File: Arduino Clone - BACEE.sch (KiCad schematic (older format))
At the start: 13 parts, among them U1 24LC1025, U2 24LC1025, U3 DS1337_AF, U4 ATMEGA328P-AU, Y1 Crystal, Y2 Crystal

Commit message: associations
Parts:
- BT1: value Battery -> Battery 3V; footprint (none) -> Connector_PinHeader_2.54mm:PinHeader_1x02_P2.54mm_Vertical
- C1, C2: value C -> 22pF; footprint (none) -> Capacitor_SMD:C_0805_2012Metric_Pad1.15x1.40mm_HandSolder
- C3: value CP -> 10uF; footprint (none) -> Capacitor_SMD:C_0805_2012Metric_Pad1.15x1.40mm_HandSolder
- D1: footprint (none) -> LED_SMD:LED_0805_2012Metric_Pad1.15x1.40mm_HandSolder
- R1: value R -> 330Ohms; footprint (none) -> Resistor_SMD:R_0805_2012Metric_Pad1.15x1.40mm_HandSolder
- R2: value R -> 10kOhms; footprint (none) -> Resistor_SMD:R_0805_2012Metric_Pad1.15x1.40mm_HandSolder
- U1, U2: footprint (none) -> Package_SO:SOIJ-8_5.3x5.3mm_P1.27mm
- U3: value DS1337_AF -> DS13375+; footprint (none) -> Package_SO:SO-8_5.3x6.2mm_P1.27mm
- Y1: value Crystal -> Crystal 32Mhz; footprint (none) -> Crystal:Crystal_SMD_MicroCrystal_CC7V-T1A-2Pin_3.2x1.5mm
- Y2: value Crystal -> Crystal 16Mhz; footprint (none) -> Crystal:Crystal_SMD_5032-2Pin_5.0x3.2mm_HandSoldering
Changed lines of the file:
@@
 P 9100 2250
 F 0 "BT1" H 9208 2296 50  0000 L CNN
-F 1 "Battery" H 9208 2205 50  0000 L CNN
-F 2 "" V 9100 2310 50  0001 C CNN
+F 1 "Battery 3V" H 9208 2205 50  0000 L CNN
+F 2 "Connector_PinHeader_2.54mm:PinHeader_1x02_P2.54mm_Vertical" V 9100 2310 50  0001 C CNN
 F 3 "~" V 9100 2310 50  0001 C CNN
 	1    9100 2250
@@
 P 5300 1850
 F 0 "C1" H 5415 1896 50  0000 L CNN
-F 1 "C" H 5415 1805 50  0000 L CNN
-F 2 "" H 5338 1700 50  0001 C CNN
+F 1 "22pF" H 5415 1805 50  0000 L CNN
+F 2 "Capacitor_SMD:C_0805_2012Metric_Pad1.15x1.40mm_HandSolder" H 5338 1700 50  0001 C CNN
 F 3 "~" H 5300 1850 50  0001 C CNN
 	1    5300 1850
@@
 P 5300 2250
 F 0 "C2" H 5415 2296 50  0000 L CNN
-F 1 "C" H 5415 2205 50  0000 L CNN
-F 2 "" H 5338 2100 50  0001 C CNN
+F 1 "22pF" H 5415 2205 50  0000 L CNN
+F 2 "Capacitor_SMD:C_0805_2012Metric_Pad1.15x1.40mm_HandSolder" H 5338 2100 50  0001 C CNN
 F 3 "~" H 5300 2250 50  0001 C CNN
 	1    5300 2250
@@
 P 9600 3100
 F 0 "C3" H 9718 3146 50  0000 L CNN
-F 1 "CP" H 9718 3055 50  0000 L CNN
-F 2 "" H 9638 2950 50  0001 C CNN
+F 1 "10uF" H 9718 3055 50  0000 L CNN
+F 2 "Capacitor_SMD:C_0805_2012Metric_Pad1.15x1.40mm_HandSolder" H 9638 2950 50  0001 C CNN
 F 3 "~" H 9600 3100 50  0001 C CNN
 	1    9600 3100
@@
 F 0 "D1" H 5843 2866 50  0000 C CNN
 F 1 "LED" H 5843 2775 50  0000 C CNN
-F 2 "" H 5850 2650 50  0001 C CNN
+F 2 "LED_SMD:LED_0805_2012Metric_Pad1.15x1.40mm_HandSolder" H 5850 2650 50  0001 C CNN
 F 3 "~" H 5850 2650 50  0001 C CNN
 	1    5850 2650
@@
 P 5400 2950
 F 0 "R1" H 5470 2996 50  0000 L CNN
-F 1 "R" H 5470 2905 50  0000 L CNN
-F 2 "" V 5330 2950 50  0001 C CNN
+F 1 "330Ohms" H 5470 2905 50  0000 L CNN
+F 2 "Resistor_SMD:R_0805_2012Metric_Pad1.15x1.40mm_HandSolder" V 5330 2950 50  0001 C CNN
 F 3 "~" H 5400 2950 50  0001 C CNN
 	1    5400 2950
@@
 P 5400 3350
 F 0 "R2" H 5470 3396 50  0000 L CNN
-F 1 "R" H 5470 3305 50  0000 L CNN
-F 2 "" V 5330 3350 50  0001 C CNN
+F 1 "10kOhms" H 5470 3305 50  0000 L CNN
+F 2 "Resistor_SMD:R_0805_2012Metric_Pad1.15x1.40mm_HandSolder" V 5330 3350 50  0001 C CNN
 F 3 "~" H 5400 3350 50  0001 C CNN
 	1    5400 3350
@@
 F 0 "U1" H 2100 5831 50  0000 C CNN
 F 1 "24LC1025" H 2100 5740 50  0000 C CNN
-F 2 "" H 2100 5350 50  0001 C CNN
+F 2 "Package_SO:SOIJ-8_5.3x5.3mm_P1.27mm" H 2100 5350 50  0001 C CNN
 F 3 "http://ww1.microchip.com/downloads/en/DeviceDoc/21941B.pdf" H 2100 5350 50  0001 C CNN
 	1    2100 5350
@@
 P 2550 2250
 F 0 "U3" H 2525 2881 50  0000 C CNN
-F 1 "DS1337_AF" H 2525 2790 50  0000 C CNN
-F 2 "" H 2550 2250 50  0001 C CNN
+F 1 "DS13375+" H 2525 2790 50  0000 C CNN
+F 2 "Package_SO:SO-8_5.3x6.2mm_P1.27mm" H 2550 2250 50  0001 C CNN
 F 3 "https://datasheets.maximintegrated.com/en/ds/DS1337-DS1337C.pdf" H 2550 2250 50  0001 C CNN
 	1    2550 2250
@@
 P 1600 2000
 F 0 "Y1" H 1600 2268 50  0000 C CNN
-F 1 "Crystal" H 1600 2177 50  0000 C CNN
-F 2 "" H 1600 2000 50  0001 C CNN
+F 1 "Crystal 32Mhz" H 1600 2177 50  0000 C CNN
+F 2 "Crystal:Crystal_SMD_MicroCrystal_CC7V-T1A-2Pin_3.2x1.5mm" H 1600 2000 50  0001 C CNN
 F 3 "~" H 1600 2000 50  0001 C CNN
 	1    1600 2000
@@
 P 5750 2100
 F 0 "Y2" V 5704 2231 50  0000 L CNN
-F 1 "Crystal" V 5795 2231 50  0000 L CNN
-F 2 "" H 5750 2100 50  0001 C CNN
+F 1 "Crystal 16Mhz" V 5795 2231 50  0000 L CNN
+F 2 "Crystal:Crystal_SMD_5032-2Pin_5.0x3.2mm_HandSoldering" H 5750 2100 50  0001 C CNN
 F 3 "~" H 5750 2100 50  0001 C CNN
 	1    5750 2100
@@
 F 0 "U2" H 2100 6981 50  0000 C CNN
 F 1 "24LC1025" H 2100 6890 50  0000 C CNN
-F 2 "" H 2100 6500 50  0001 C CNN
+F 2 "Package_SO:SOIJ-8_5.3x5.3mm_P1.27mm" H 2100 6500 50  0001 C CNN
 F 3 "http://ww1.microchip.com/downloads/en/DeviceDoc/21941B.pdf" H 2100 6500 50  0001 C CNN
 	1    2100 6500

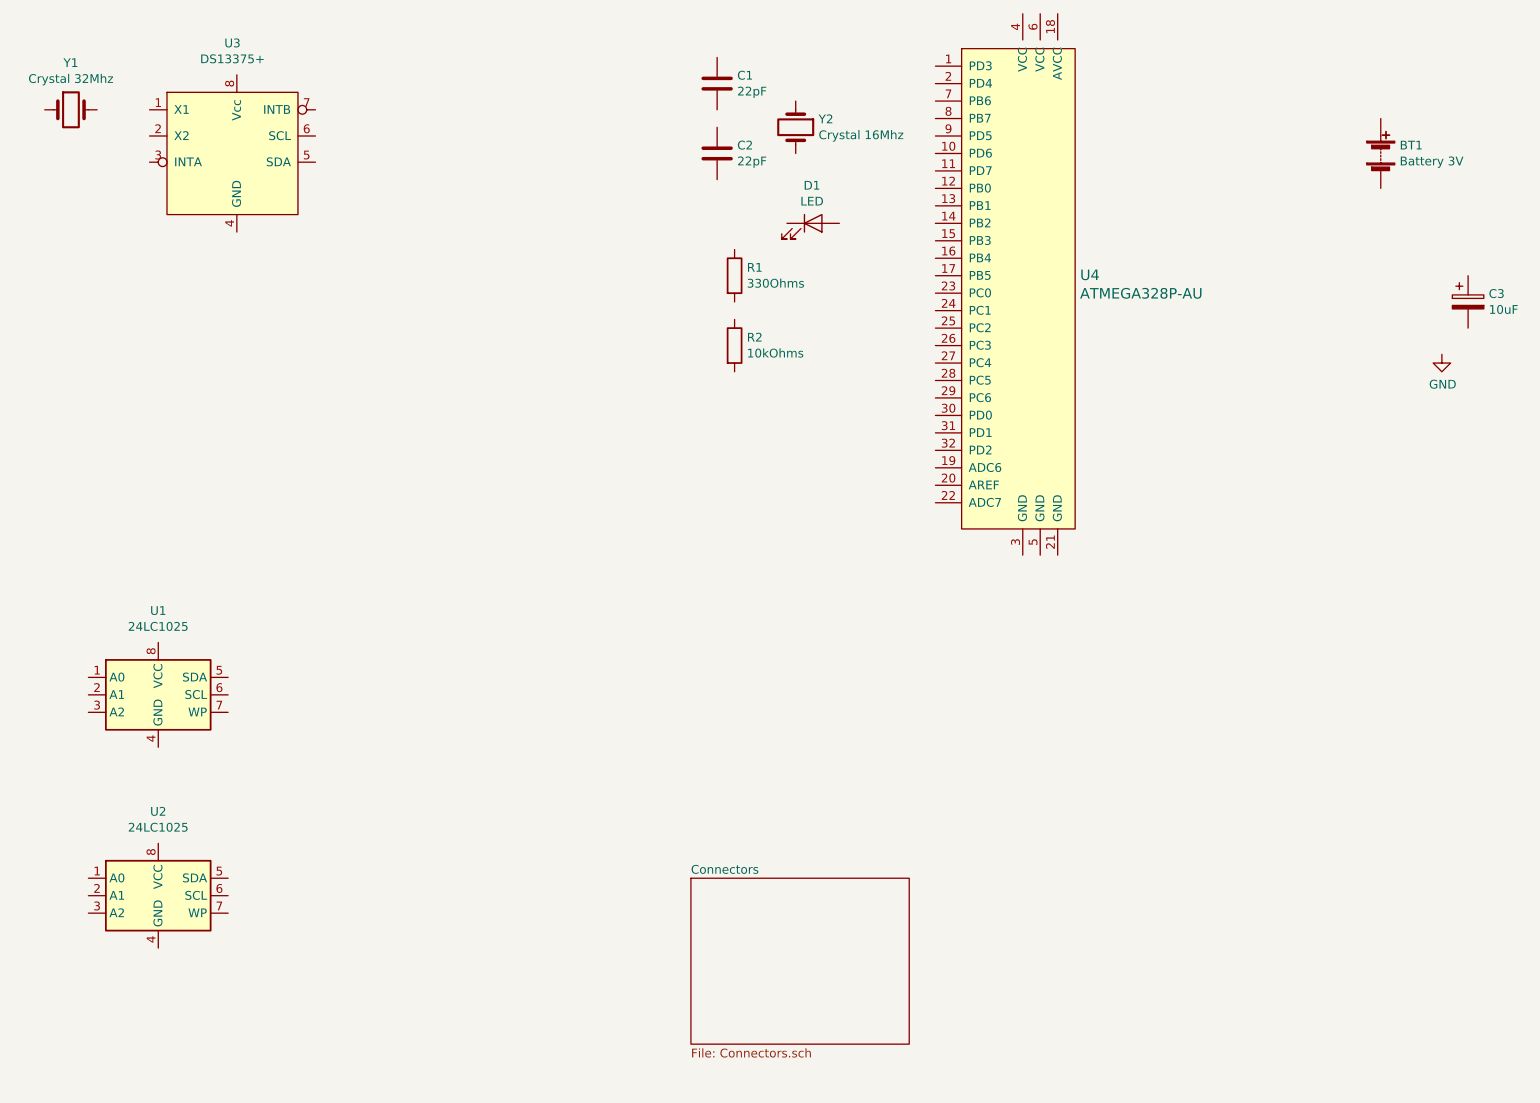
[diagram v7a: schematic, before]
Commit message: Completed wiring in connectors
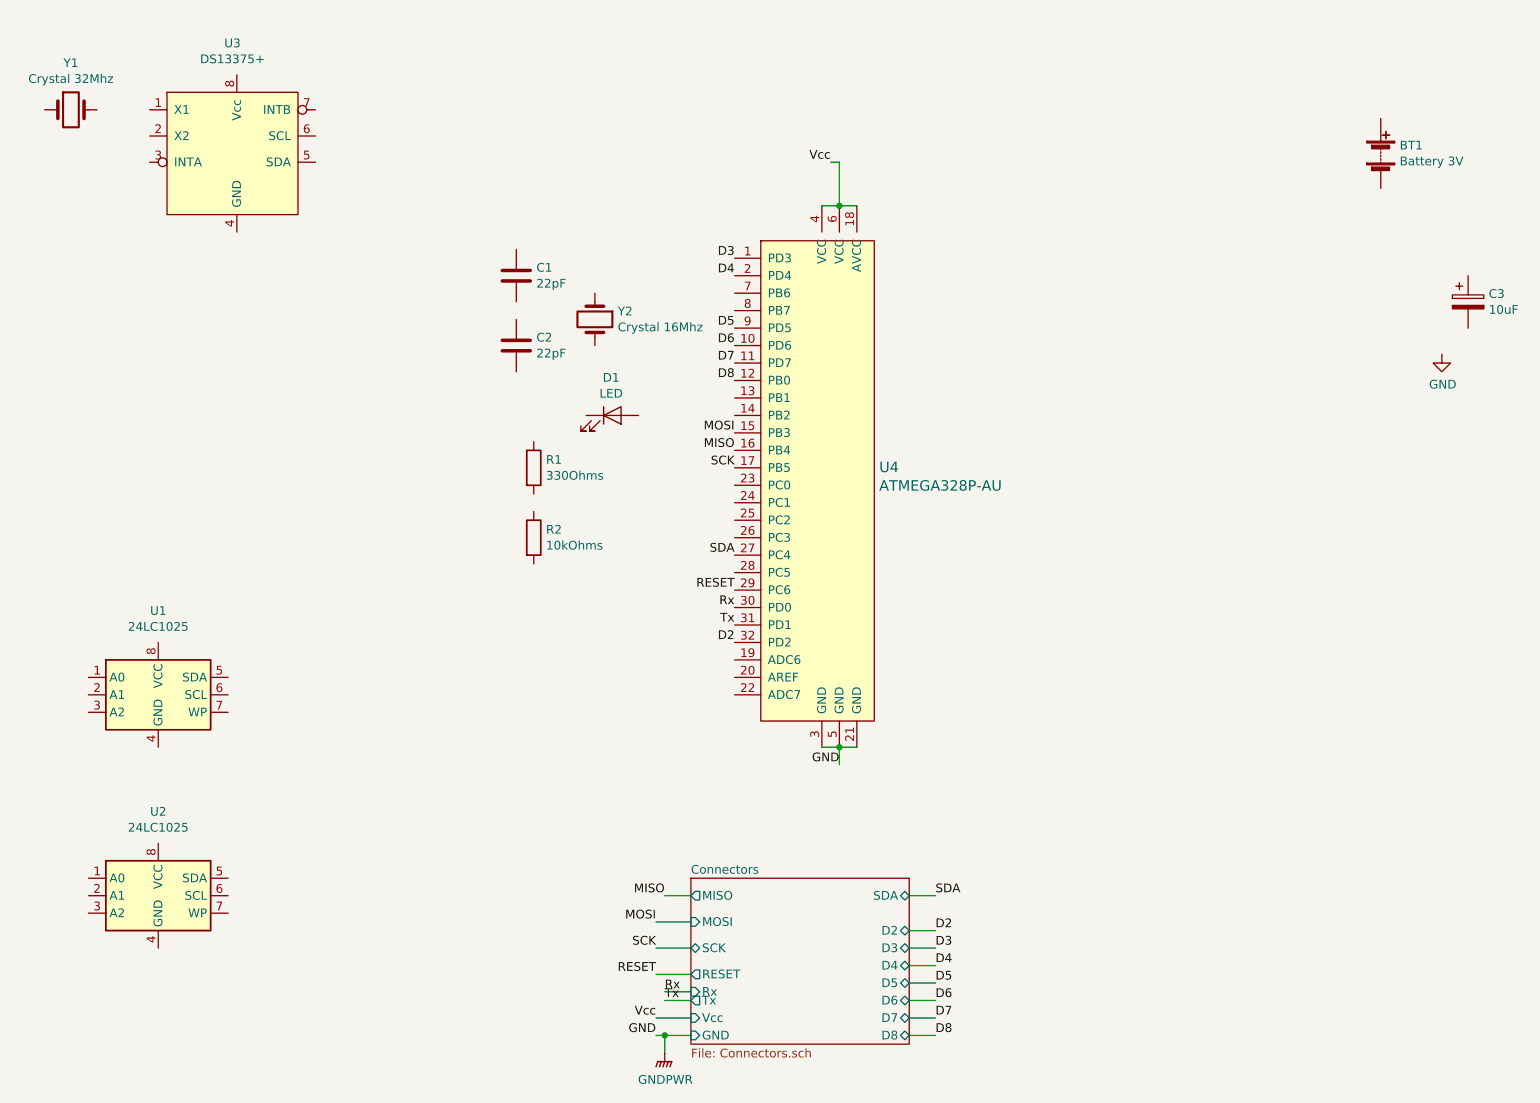
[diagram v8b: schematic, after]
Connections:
- net GND: now also U4.21 (GND), U4.3 (GND), U4.5 (GND)
- net D3: now reaches U4.1 (PD3)
- net D6: now reaches U4.10 (PD6)
- net D7: now reaches U4.11 (PD7)
- net D8: now reaches U4.12 (PB0)
- net MOSI: now reaches U4.15 (PB3)
- net MISO: now reaches U4.16 (PB4)
- net SCK: now reaches U4.17 (PB5)
- net Vcc: now reaches U4.18 (AVCC)
- net Vcc: now also U4.4 (VCC), U4.6 (VCC)
- net D4: now reaches U4.2 (PD4)
- net SDA: now reaches U4.27 (PC4)
- net RESET: now reaches U4.29 (PC6)
- net Rx: now reaches U4.30 (PD0)
- net Tx: now reaches U4.31 (PD1)
- net D2: now reaches U4.32 (PD2)
- net D5: now reaches U4.9 (PD5)
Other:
- moved on the sheet: C1, C2, D1, R1, R2, U4, Y2
